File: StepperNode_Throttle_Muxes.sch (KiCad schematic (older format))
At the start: 6 parts, among them P2 TE_640456-8, P3 TE_640456-8, U2 MAX4948ETG+, U3 MAX4948ETG+

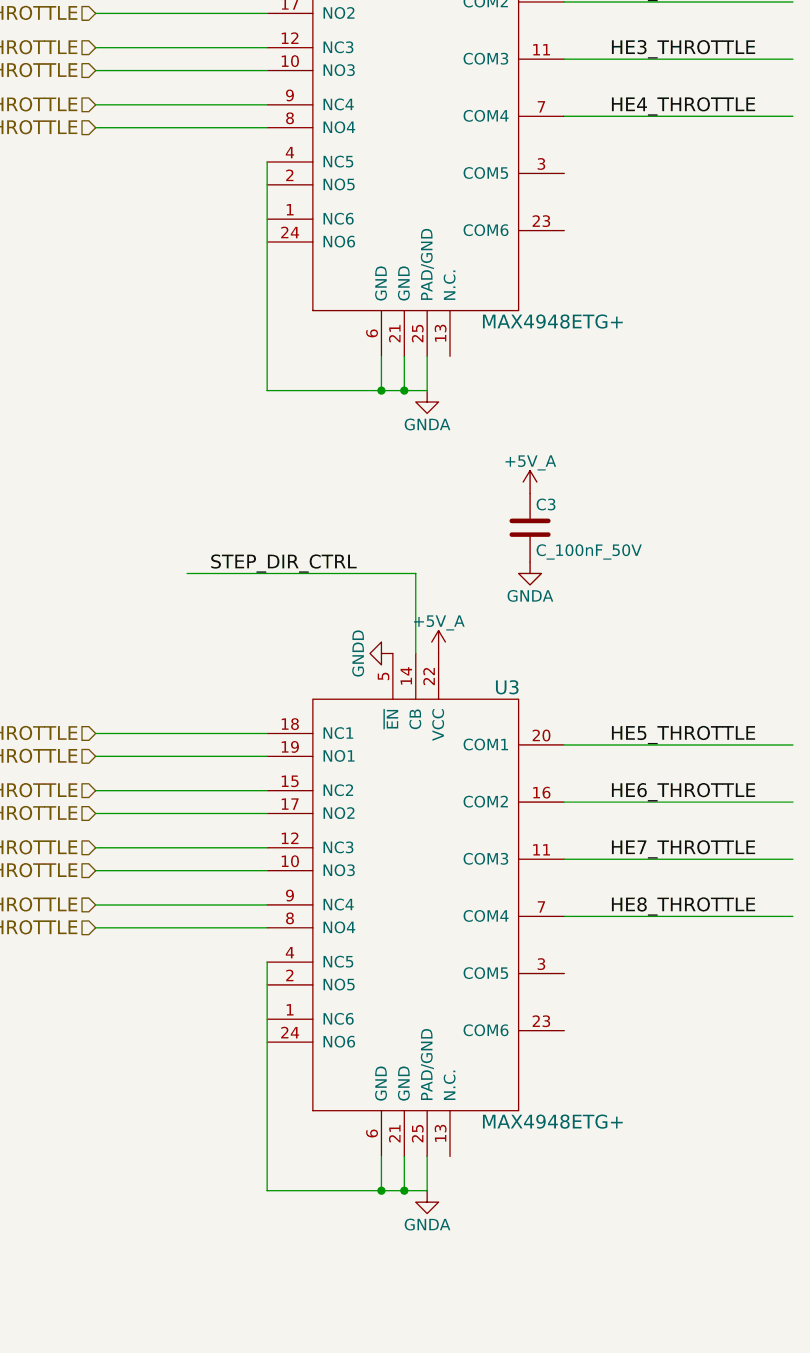
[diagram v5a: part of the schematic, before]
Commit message: Fix most ERC warnings (non-connected pins, etc)
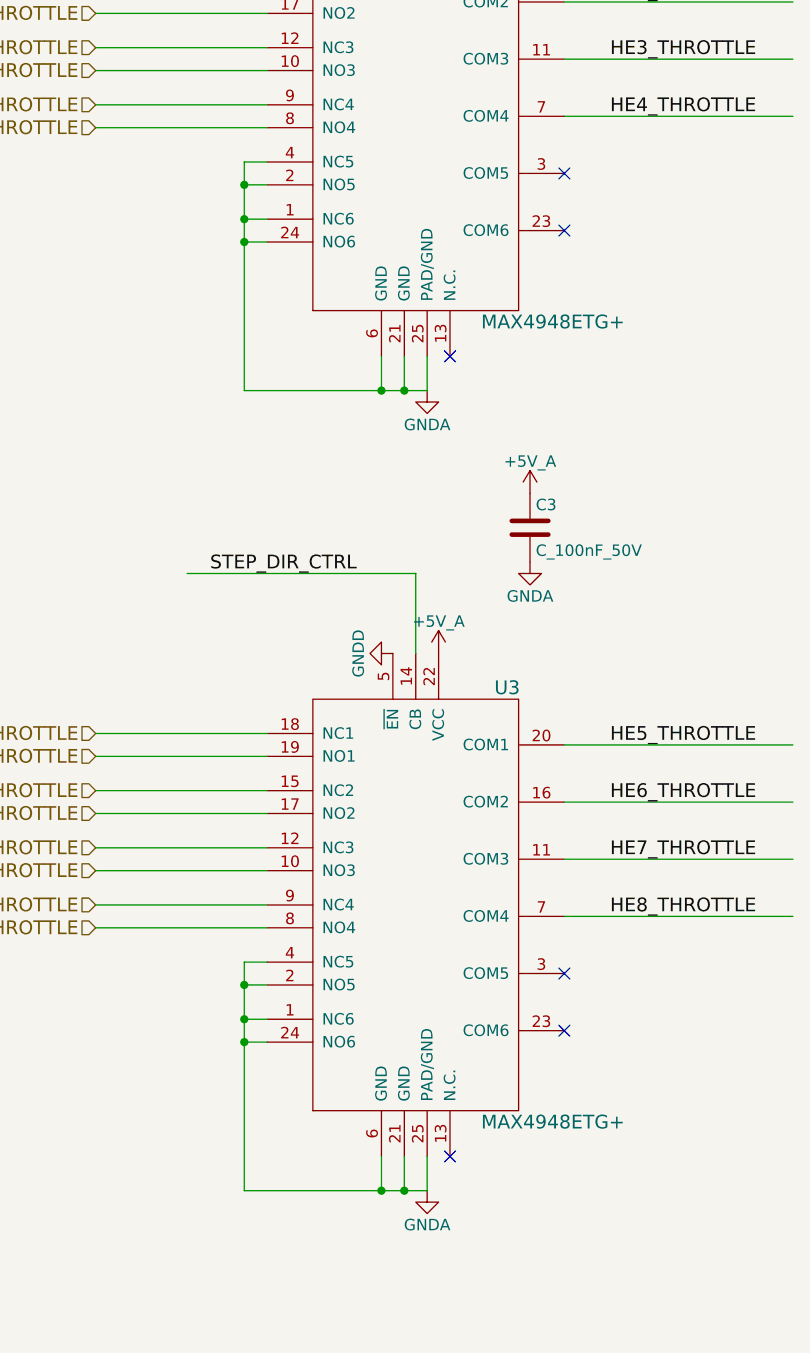
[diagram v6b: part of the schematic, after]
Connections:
- wire segments 56 -> 64
- no-connect marks 0 -> 6
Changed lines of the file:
@@
 STEP_DIR_CTRL
 $Comp
-L GNDD #PWR8
+L GNDD #PWR08
 U 1 1 57569516
 P 7050 1850
-F 0 "#PWR8" H 7050 1600 50  0001 C CNN
+F 0 "#PWR08" H 7050 1600 50  0001 C CNN
 F 1 "GNDD" H 7050 1700 50  0000 C CNN
 F 2 "" H 7050 1850 50  0000 C CNN
@@
 High = NO Channel
 $Comp
-L GNDA #PWR15
+L GNDA #PWR09
 U 1 1 5756951F
 P 7650 1450
-F 0 "#PWR15" H 7650 1200 50  0001 C CNN
+F 0 "#PWR09" H 7650 1200 50  0001 C CNN
 F 1 "GNDA" H 7650 1300 50  0000 C CNN
 F 2 "" H 7650 1450 50  0000 C CNN
@@
 $EndComp
 $Comp
-L GNDD #PWR9
+L GNDD #PWR010
 U 1 1 575696A3
 P 7050 5350
-F 0 "#PWR9" H 7050 5100 50  0001 C CNN
+F 0 "#PWR010" H 7050 5100 50  0001 C CNN
 F 1 "GNDD" H 7050 5200 50  0000 C CNN
 F 2 "" H 7050 5350 50  0000 C CNN
@@
 	7150 5000 6150 5000
 $Comp
-L GNDA #PWR17
+L GNDA #PWR011
 U 1 1 575696AC
 P 7650 4950
-F 0 "#PWR17" H 7650 4700 50  0001 C CNN
+F 0 "#PWR011" H 7650 4700 50  0001 C CNN
 F 1 "GNDA" H 7650 4800 50  0000 C CNN
 F 2 "" H 7650 4950 50  0000 C CNN
@@
 STEP_DIR_CTRL
 $Comp
-L GNDA #PWR11
+L GNDA #PWR012
 U 1 1 57569B4E
 P 7200 7700
-F 0 "#PWR11" H 7200 7450 50  0001 C CNN
+F 0 "#PWR012" H 7200 7450 50  0001 C CNN
 F 1 "GNDA" H 7200 7550 50  0000 C CNN
 F 2 "" H 7200 7700 50  0000 C CNN
@@
 $EndComp
 Wire Wire Line
-	6500 6700 6500 7700
-Wire Wire Line
-	6500 7700 7200 7700
+	6400 7700 7200 7700
 Wire Wire Line
 	7000 7550 7000 7700
@@
 	7200 7700 7200 7550
 $Comp
-L GNDA #PWR10
+L GNDA #PWR013
 U 1 1 57569C1E
 P 7200 4200
-F 0 "#PWR10" H 7200 3950 50  0001 C CNN
+F 0 "#PWR013" H 7200 3950 50  0001 C CNN
 F 1 "GNDA" H 7200 4050 50  0000 C CNN
 F 2 "" H 7200 4200 50  0000 C CNN
@@
 $EndComp
 Wire Wire Line
-	7200 4200 6500 4200
-Wire Wire Line
-	6500 4200 6500 3200
-Wire Wire Line
-	7200 4050 7200 4200
+	6400 4200 7200 4200
+Wire Wire Line
+	7200 4200 7200 4050
 Wire Wire Line
 	7100 4050 7100 4200
@@
 $EndComp
 $Comp
-L +5V_A #PWR14
+L +5V_A #PWR014
 U 1 1 57672F62
 P 7650 1150
-F 0 "#PWR14" H 7650 1000 50  0001 C CNN
+F 0 "#PWR014" H 7650 1000 50  0001 C CNN
 F 1 "+5V_A" H 7650 1290 50  0000 C CNN
 F 2 "" H 7650 1150 60  0000 C CNN
@@
 $EndComp
 $Comp
-L +5V_A #PWR12
+L +5V_A #PWR015
 U 1 1 57672F82
 P 7250 1850
-F 0 "#PWR12" H 7250 1700 50  0001 C CNN
+F 0 "#PWR015" H 7250 1700 50  0001 C CNN
 F 1 "+5V_A" H 7250 1990 50  0000 C CNN
 F 2 "" H 7250 1850 60  0000 C CNN
@@
 $EndComp
 $Comp
-L +5V_A #PWR16
+L +5V_A #PWR016
 U 1 1 5767309E
 P 7650 4650
-F 0 "#PWR16" H 7650 4500 50  0001 C CNN
+F 0 "#PWR016" H 7650 4500 50  0001 C CNN
 F 1 "+5V_A" H 7650 4790 50  0000 C CNN
 F 2 "" H 7650 4650 60  0000 C CNN
@@
 $EndComp
 $Comp
-L +5V_A #PWR13
+L +5V_A #PWR017
 U 1 1 576730BE
 P 7250 5350
-F 0 "#PWR13" H 7250 5200 50  0001 C CNN
+F 0 "#PWR017" H 7250 5200 50  0001 C CNN
 F 1 "+5V_A" H 7250 5490 50  0000 C CNN
 F 2 "" H 7250 5350 60  0000 C CNN
@@
 $EndComp
 $Comp
-L GNDA #PWR?
+L GNDA #PWR018
 U 1 1 575D0F3B
 P 10950 6350
-F 0 "#PWR?" H 10950 6100 50  0001 C CNN
+F 0 "#PWR018" H 10950 6100 50  0001 C CNN
 F 1 "GNDA" H 10950 6200 50  0000 C CNN
 F 2 "" H 10950 6350 50  0000 C CNN
@@
 Connection ~ 10950 5850
 $Comp
-L GNDA #PWR?
+L GNDA #PWR019
 U 1 1 575D10B7
 P 10950 2850
-F 0 "#PWR?" H 10950 2600 50  0001 C CNN
+F 0 "#PWR019" H 10950 2600 50  0001 C CNN
 F 1 "GNDA" H 10950 2700 50  0000 C CNN
 F 2 "" H 10950 2850 50  0000 C CNN
@@
 	11000 2750 10950 2750
 Connection ~ 10950 2750
+Wire Wire Line
+	6500 3200 6400 3200
+Wire Wire Line
+	6400 3200 6400 4200
+Wire Wire Line
+	6500 3300 6400 3300
+Connection ~ 6400 3300
+Wire Wire Line
+	6400 3450 6500 3450
+Connection ~ 6400 3450
+Wire Wire Line
+	6500 3550 6400 3550
+Connection ~ 6400 3550
+NoConn ~ 7300 4050
+NoConn ~ 7800 3250
+NoConn ~ 7800 3500
+Wire Wire Line
+	6500 6700 6400 6700
+Wire Wire Line
+	6400 6700 6400 7700
+Wire Wire Line
+	6500 6800 6400 6800
+Connection ~ 6400 6800
+Wire Wire Line
+	6400 6950 6500 6950
+Connection ~ 6400 6950
+Wire Wire Line
+	6500 7050 6400 7050
+Connection ~ 6400 7050
+NoConn ~ 7300 7550
+NoConn ~ 7800 6750
+NoConn ~ 7800 7000
 $EndSCHEMATC

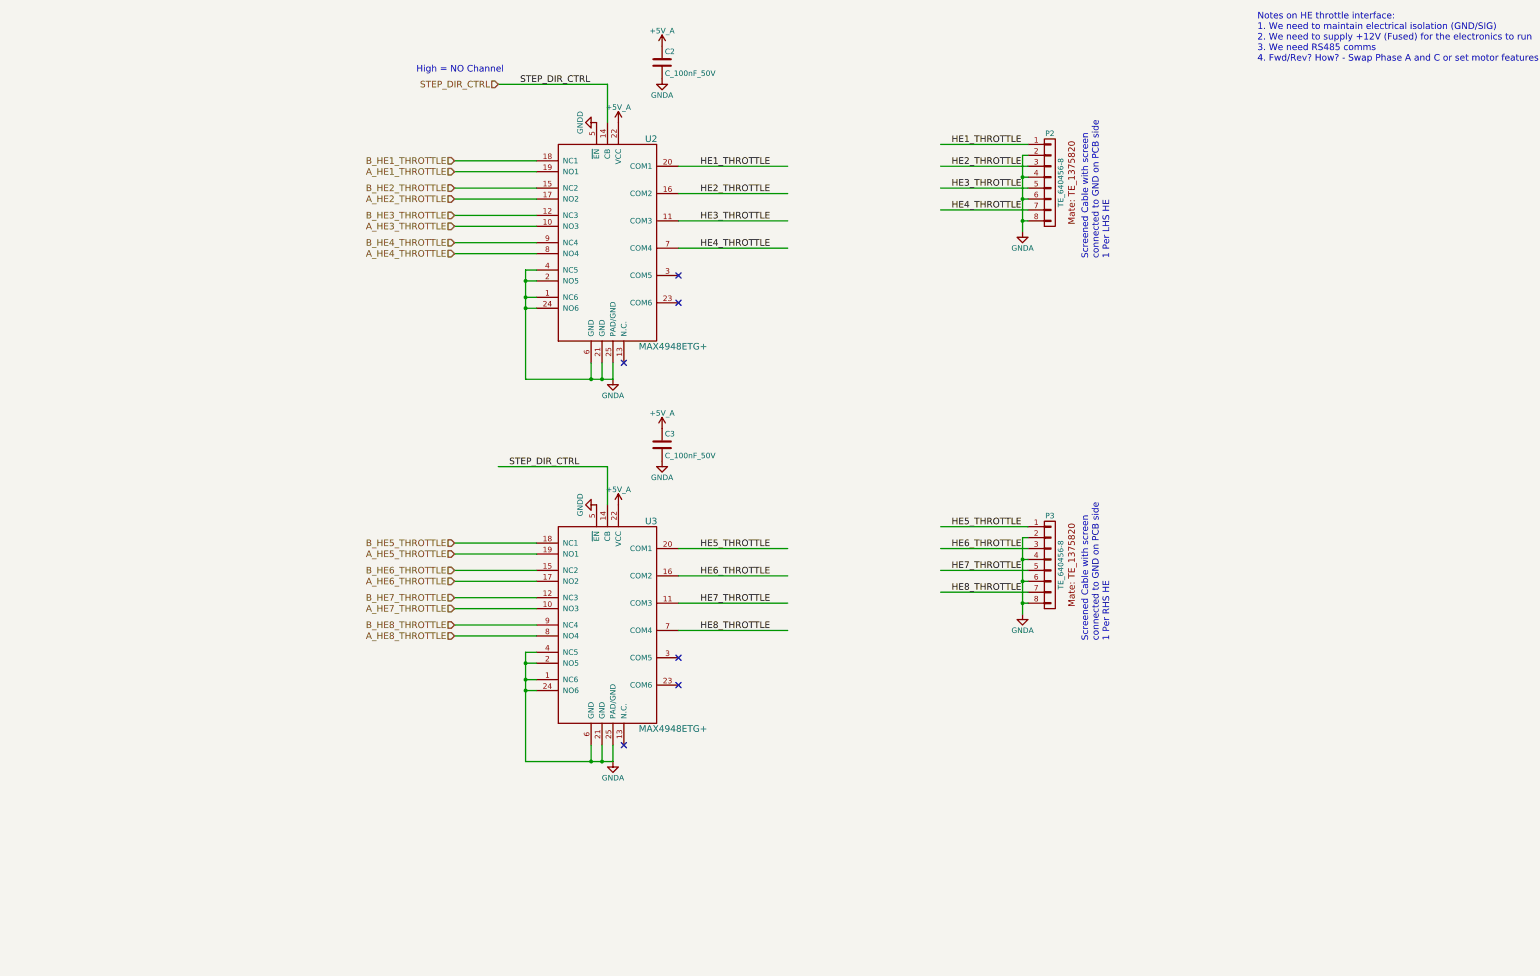
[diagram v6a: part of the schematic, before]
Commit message: Update Teensy IO and place isolation amp.
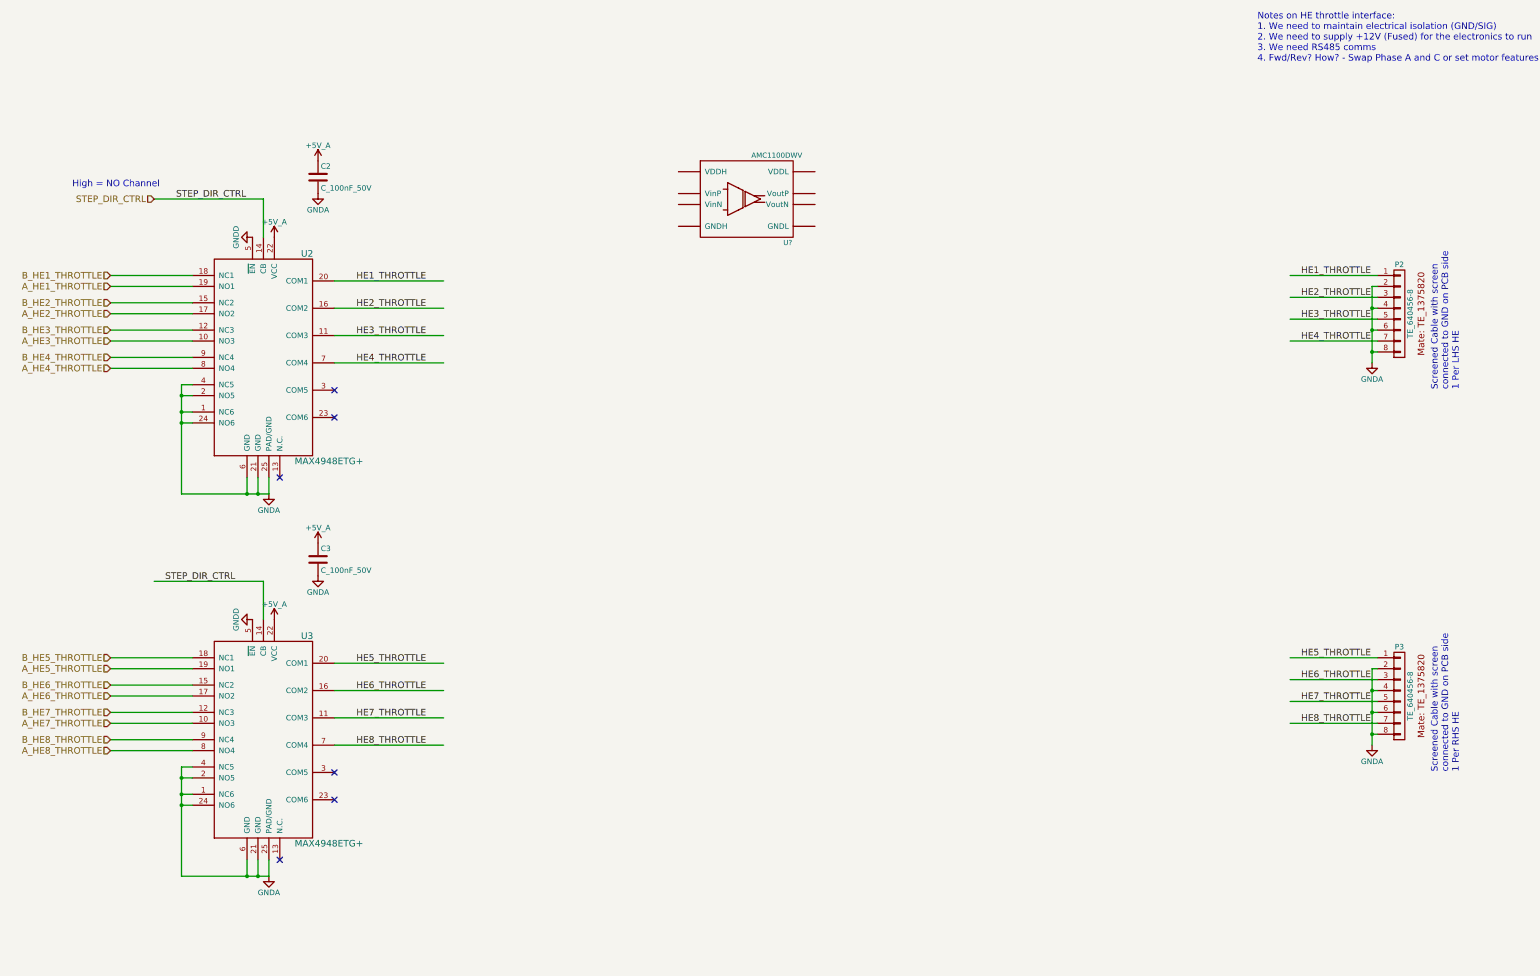
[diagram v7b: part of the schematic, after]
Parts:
- added U?: AMC1100DWV, RLOOP_FOOTPRINTS:rLoop_SOIC8, symbol AMC1100DWV
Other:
- moved on the sheet: C2, C3, P2, P3, U2, U3
